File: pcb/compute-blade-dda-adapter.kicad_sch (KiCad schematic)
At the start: 2 parts, among them J1 COMPUTE BLADE, J2 DDA GPS/RTC

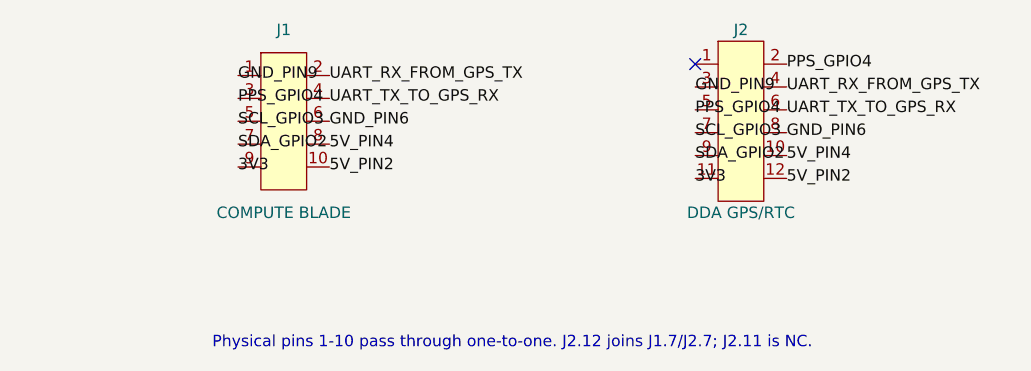
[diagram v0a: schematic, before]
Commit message: Add upright DDA mechanical revision
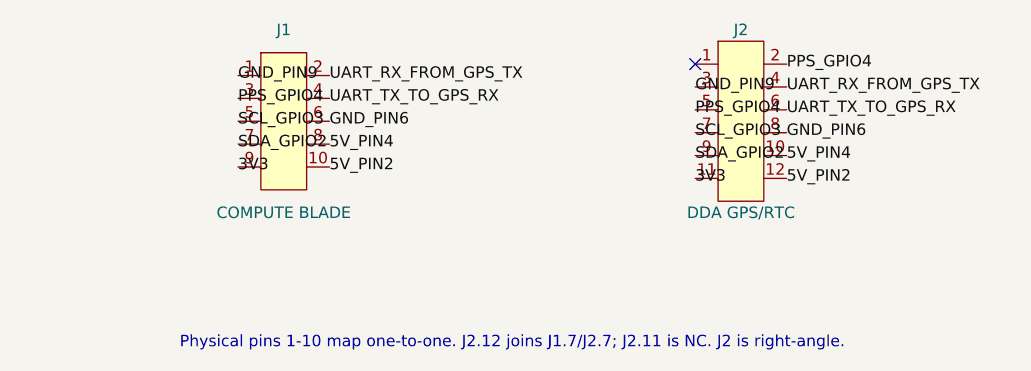
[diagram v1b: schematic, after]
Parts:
- J2: footprint Connector_PinHeader_2.54mm:PinHeader_2x06_P2.54mm_Vertical -> Connector_PinHeader_2.54mm:PinHeader_2x06_P2.54mm_Horizontal
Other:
- note added: "Physical pins 1-10 map one-to-one. J2.12 joins J1.7/J2.7; J2.11 is NC. J2 is right-angle."
- note removed: "Physical pins 1-10 pass through one-to-one. J2.12 joins J1.7/J2.7; J2.11 is NC."
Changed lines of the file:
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@@
   (title_block
     (title "Compute Blade to DDA GPS/RTC passive adapter")
-    (date "2026-09-20")
-    (rev "0.1")
+    (date "2026-09-21")
+    (rev "0.2")
     (company "Open hardware reference design")
     (comment 1 "PHYSICAL HEADER PIN NUMBERS ONLY"))
@@
     (property "Reference" "J2" (at 111.76 66.04 0) (effects (font (size 1.27 1.27))))
     (property "Value" "DDA GPS/RTC" (at 111.76 86.36 0) (effects (font (size 1.27 1.27))))
-    (property "Footprint" "Connector_PinHeader_2.54mm:PinHeader_2x06_P2.54mm_Vertical" (at 111.76 76.20 0) (effects (font (size 1.27 1.27)) hide))
+    (property "Footprint" "Connector_PinHeader_2.54mm:PinHeader_2x06_P2.54mm_Horizontal" (at 111.76 76.20 0) (effects (font (size 1.27 1.27)) hide))
     (property "Datasheet" "~" (at 111.76 76.20 0) (effects (font (size 1.27 1.27)) hide))
     (property "Description" "Physical pin numbering; do not reinterpret as BCM numbering" (at 111.76 76.20 0) (effects (font (size 1.27 1.27)) hide))
@@
         (path "/42308dc1-1a86-53d5-952a-65642bf70d9f" (reference "J2") (unit 1))))
   )
-  (text "Physical pins 1-10 pass through one-to-one. J2.12 joins J1.7/J2.7; J2.11 is NC."
+  (text "Physical pins 1-10 map one-to-one. J2.12 joins J1.7/J2.7; J2.11 is NC. J2 is right-angle."
     (exclude_from_sim no) (at 86.36 101.60 0)
     (effects (font (size 1.27 1.27)) (justify bottom)))

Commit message: Redesign adapter for parallel DDA stack
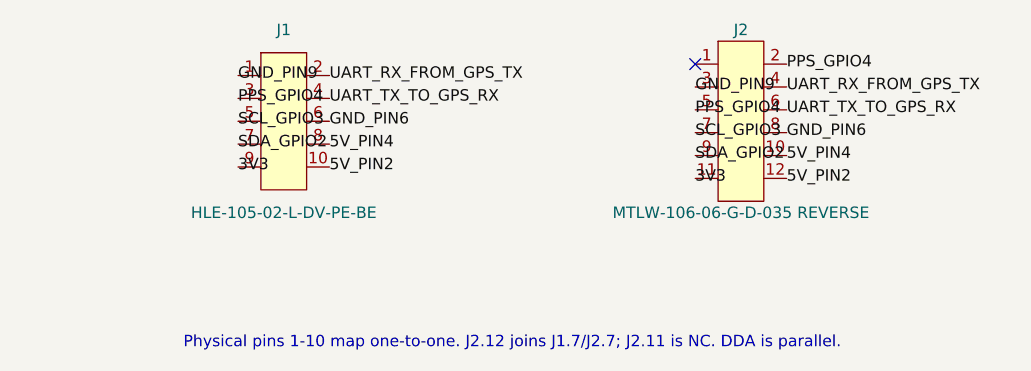
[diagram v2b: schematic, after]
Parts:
- J1: value COMPUTE BLADE -> HLE-105-02-L-DV-PE-BE; footprint Connector_PinSocket_2.54mm:PinSocket_2x05_P2.54mm_Vertical -> Adapter:Samtec_HLE-105-02-L-DV-PE-BE
- J2: value DDA GPS/RTC -> MTLW-106-06-G-D-035 REVERSE; footprint Connector_PinHeader_2.54mm:PinHeader_2x06_P2.54mm_Horizontal -> Adapter:Samtec_MTLW-106-06-G-D-035_Reverse
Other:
- note added: "Physical pins 1-10 map one-to-one. J2.12 joins J1.7/J2.7; J2.11 is NC. DDA is parallel."
- note removed: "Physical pins 1-10 map one-to-one. J2.12 joins J1.7/J2.7; J2.11 is NC. J2 is right-angle."
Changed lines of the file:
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@@
     (title "Compute Blade to DDA GPS/RTC passive adapter")
     (date "2026-09-21")
-    (rev "0.2")
+    (rev "0.3-parallel")
     (company "Open hardware reference design")
     (comment 1 "PHYSICAL HEADER PIN NUMBERS ONLY"))
@@
     (exclude_from_sim no) (in_bom yes) (on_board yes) (dnp no)
     (property "Reference" "J1" (at 60.96 66.04 0) (effects (font (size 1.27 1.27))))
-    (property "Value" "COMPUTE BLADE" (at 60.96 86.36 0) (effects (font (size 1.27 1.27))))
-    (property "Footprint" "Connector_PinSocket_2.54mm:PinSocket_2x05_P2.54mm_Vertical" (at 60.96 76.20 0) (effects (font (size 1.27 1.27)) hide))
+    (property "Value" "HLE-105-02-L-DV-PE-BE" (at 60.96 86.36 0) (effects (font (size 1.27 1.27))))
+    (property "Footprint" "Adapter:Samtec_HLE-105-02-L-DV-PE-BE" (at 60.96 76.20 0) (effects (font (size 1.27 1.27)) hide))
     (property "Datasheet" "~" (at 60.96 76.20 0) (effects (font (size 1.27 1.27)) hide))
     (property "Description" "Physical pin numbering; do not reinterpret as BCM numbering" (at 60.96 76.20 0) (effects (font (size 1.27 1.27)) hide))
@@
     (exclude_from_sim no) (in_bom yes) (on_board yes) (dnp no)
     (property "Reference" "J2" (at 111.76 66.04 0) (effects (font (size 1.27 1.27))))
-    (property "Value" "DDA GPS/RTC" (at 111.76 86.36 0) (effects (font (size 1.27 1.27))))
-    (property "Footprint" "Connector_PinHeader_2.54mm:PinHeader_2x06_P2.54mm_Horizontal" (at 111.76 76.20 0) (effects (font (size 1.27 1.27)) hide))
+    (property "Value" "MTLW-106-06-G-D-035 REVERSE" (at 111.76 86.36 0) (effects (font (size 1.27 1.27))))
+    (property "Footprint" "Adapter:Samtec_MTLW-106-06-G-D-035_Reverse" (at 111.76 76.20 0) (effects (font (size 1.27 1.27)) hide))
     (property "Datasheet" "~" (at 111.76 76.20 0) (effects (font (size 1.27 1.27)) hide))
     (property "Description" "Physical pin numbering; do not reinterpret as BCM numbering" (at 111.76 76.20 0) (effects (font (size 1.27 1.27)) hide))
@@
         (path "/42308dc1-1a86-53d5-952a-65642bf70d9f" (reference "J2") (unit 1))))
   )
-  (text "Physical pins 1-10 map one-to-one. J2.12 joins J1.7/J2.7; J2.11 is NC. J2 is right-angle."
+  (text "Physical pins 1-10 map one-to-one. J2.12 joins J1.7/J2.7; J2.11 is NC. DDA is parallel."
     (exclude_from_sim no) (at 86.36 101.60 0)
     (effects (font (size 1.27 1.27)) (justify bottom)))

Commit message: Use conventional J2 on 1.0 mm adapter
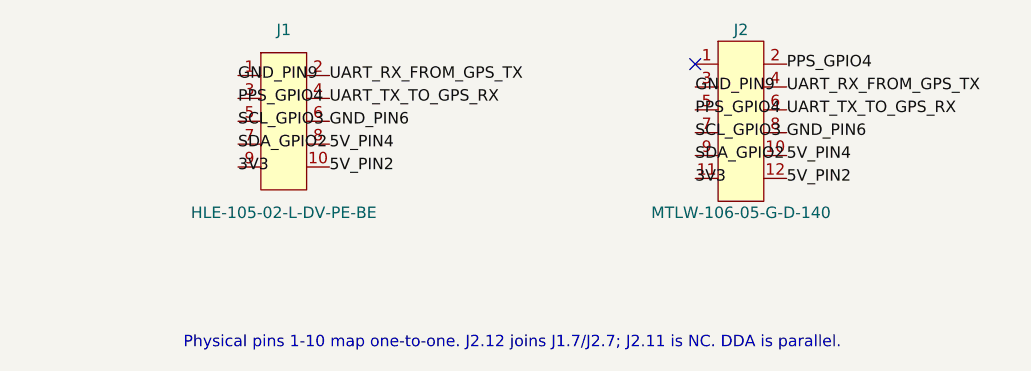
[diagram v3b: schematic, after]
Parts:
- J2: value MTLW-106-06-G-D-035 REVERSE -> MTLW-106-05-G-D-140; footprint Adapter:Samtec_MTLW-106-06-G-D-035_Reverse -> Adapter:Samtec_MTLW-106-05-G-D-140
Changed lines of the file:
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@@
     (title "Compute Blade to DDA GPS/RTC passive adapter")
     (date "2026-09-21")
-    (rev "0.3-parallel")
+    (rev "0.4-parallel-conventional")
     (company "Open hardware reference design")
     (comment 1 "PHYSICAL HEADER PIN NUMBERS ONLY"))
@@
     (exclude_from_sim no) (in_bom yes) (on_board yes) (dnp no)
     (property "Reference" "J2" (at 111.76 66.04 0) (effects (font (size 1.27 1.27))))
-    (property "Value" "MTLW-106-06-G-D-035 REVERSE" (at 111.76 86.36 0) (effects (font (size 1.27 1.27))))
-    (property "Footprint" "Adapter:Samtec_MTLW-106-06-G-D-035_Reverse" (at 111.76 76.20 0) (effects (font (size 1.27 1.27)) hide))
+    (property "Value" "MTLW-106-05-G-D-140" (at 111.76 86.36 0) (effects (font (size 1.27 1.27))))
+    (property "Footprint" "Adapter:Samtec_MTLW-106-05-G-D-140" (at 111.76 76.20 0) (effects (font (size 1.27 1.27)) hide))
     (property "Datasheet" "~" (at 111.76 76.20 0) (effects (font (size 1.27 1.27)) hide))
     (property "Description" "Physical pin numbering; do not reinterpret as BCM numbering" (at 111.76 76.20 0) (effects (font (size 1.27 1.27)) hide))
